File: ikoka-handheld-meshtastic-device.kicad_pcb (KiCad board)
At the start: 2 copper layers, 40 x 55 mm, 40 parts, among them J1 Conn_Coaxial, J4 1.25-2PWB, Q1 AO3401A, SW1 SW_Push, SW2 SW_Push, U1 MT3608, U2 E22-900M30S, U3 XIAO-nRF52840-SMD, U4 TP4056-42-ESOP8

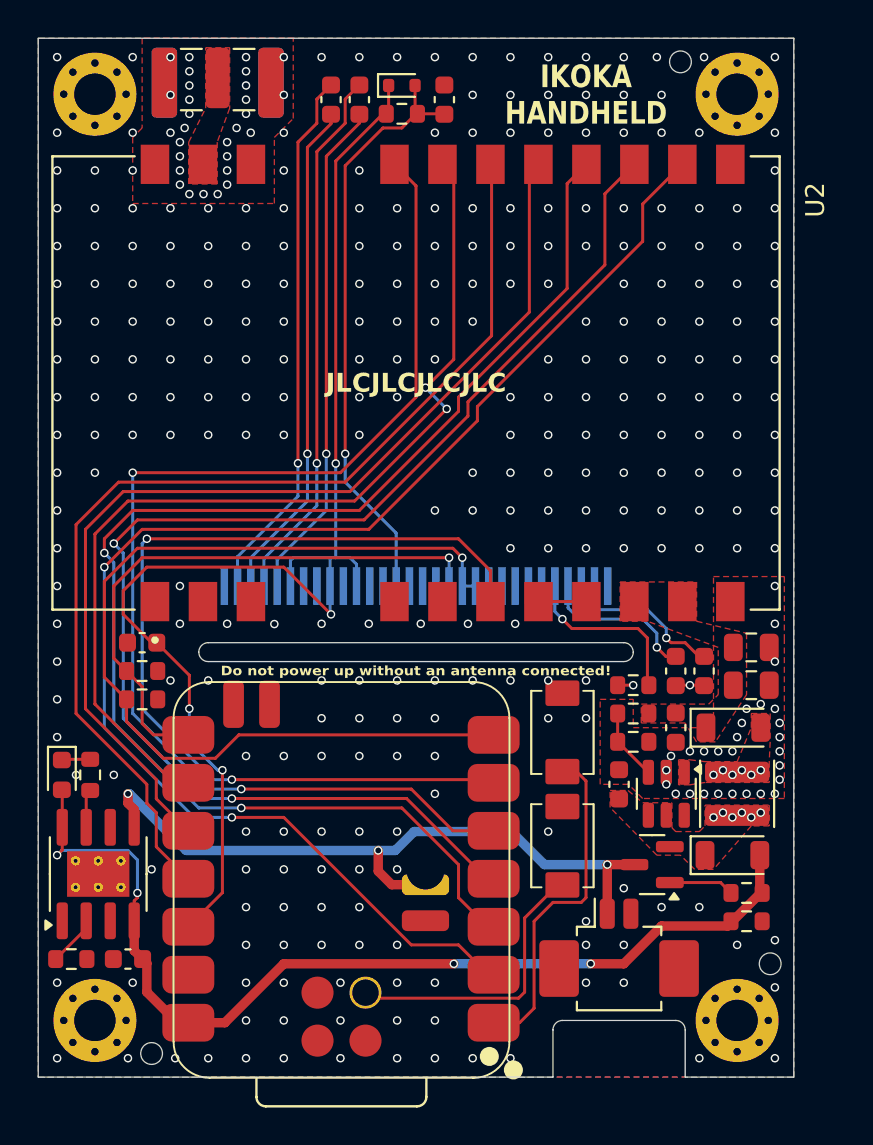
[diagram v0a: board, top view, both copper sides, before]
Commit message: fix: Add BAT output capacitor on TP4056
Signed-off-by: Andrew Yong <me@ndoo.sg>
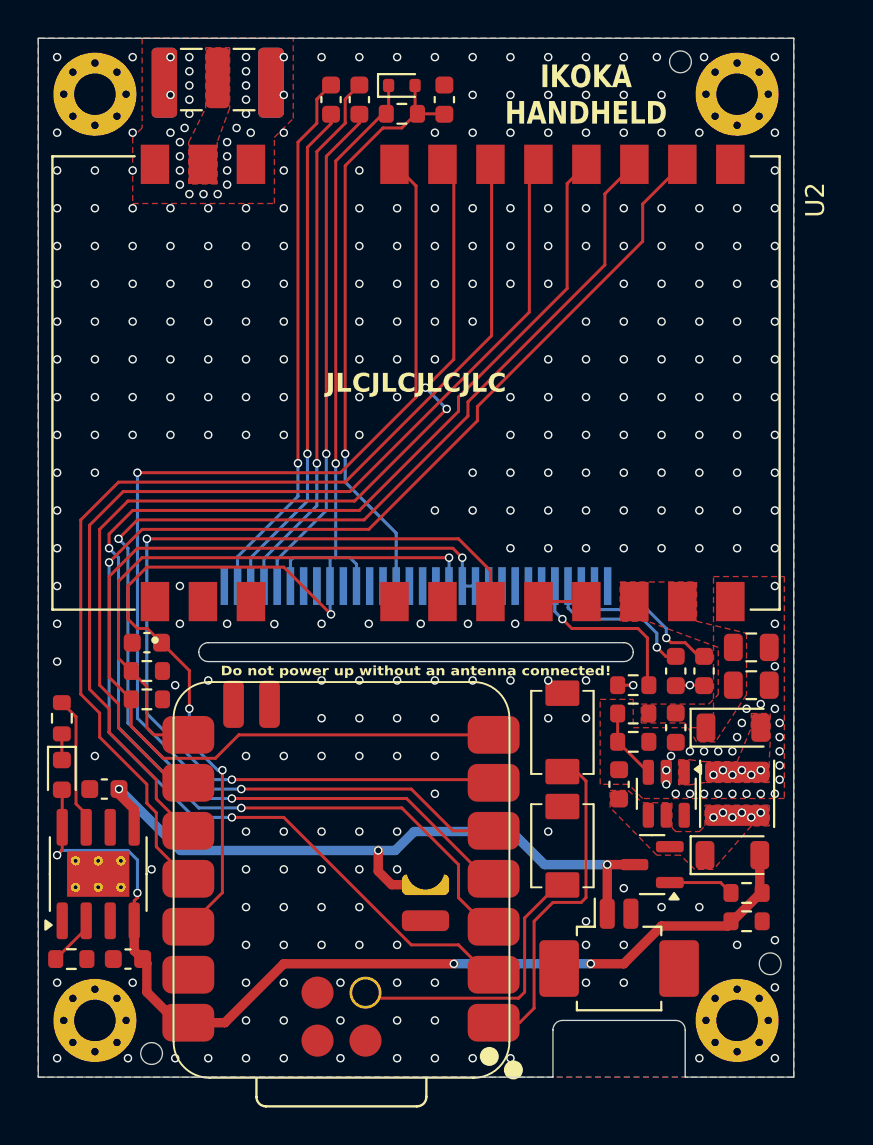
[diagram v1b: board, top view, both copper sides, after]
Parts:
- added C12: 10uF, Capacitor_SMD:C_0603_1608Metric, F.Cu at (133.5, 84.8)
- moved R10 3.35 mm to (131.2, 81.0), turned to 90 degrees
- moved C5 0.25 mm to (135.8, 77.0)
- moved R6 0.25 mm to (135.8, 80.0)
- moved R7 0.25 mm to (135.8, 78.5)
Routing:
- net Net-(U4-~{CHRG}): track 2.07 -> 7.13 mm
- net +BATT: track 37.6 -> 38.6 mm
- net GND: vias 347 -> 344

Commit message: fix: Flip SSD1306 footprint (fixes #1)
Signed-off-by: Andrew Yong <me@ndoo.sg>
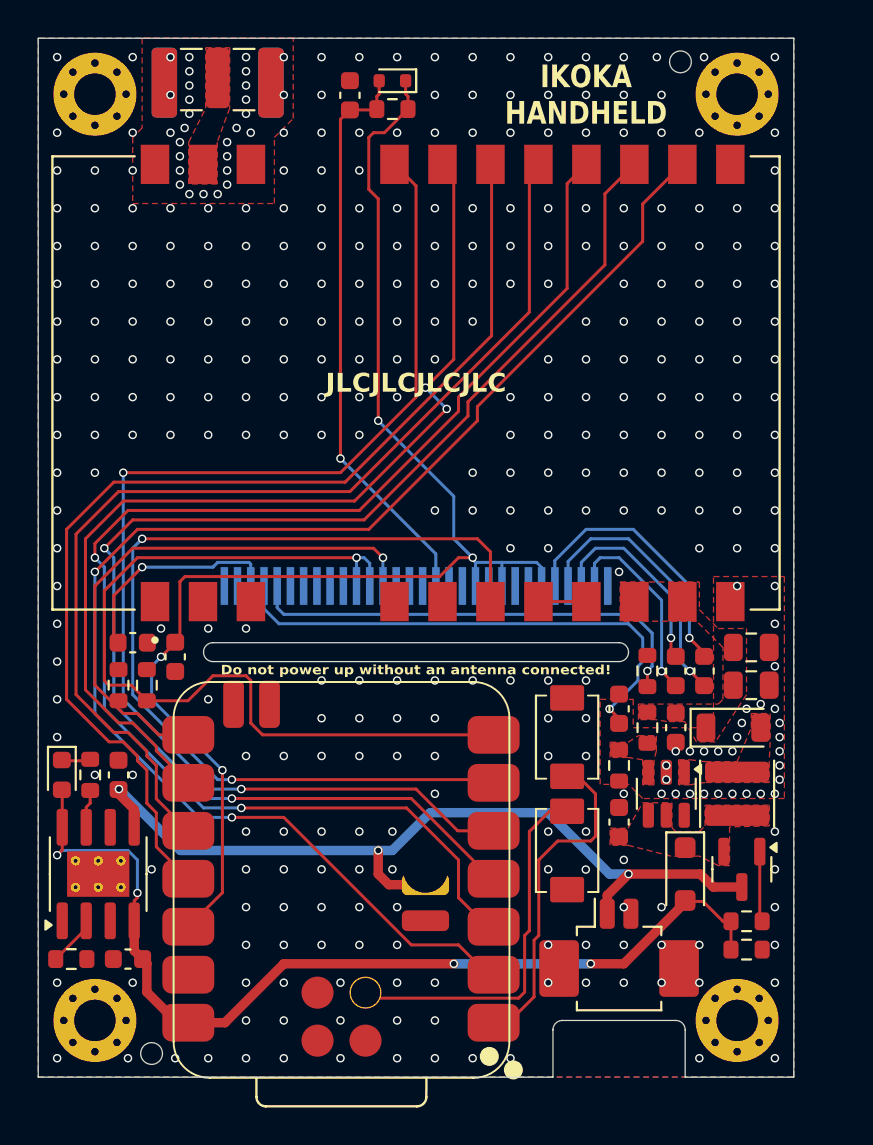
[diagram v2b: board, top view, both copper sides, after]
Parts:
- DS1: footprint Display:OLED-128O064D -> Display:OLED-128O064D_ReverseMount
- moved C8 35.3 mm to (165.2, 78.5), turned to -90 degrees
- moved C9 35.3 mm to (163.8, 78.5), turned to -90 degrees
- moved C6 30.3 mm to (135.0, 77.0), turned to 0 degrees
- moved C10 5.01 mm to (146.5, 48.0)
- moved Q1 4.76 mm to (167.2, 89.0), turned to -90 degrees
- moved C7 3.61 mm to (160.8, 80.5), turned to 90 degrees
- moved R10 3.35 mm to (132.8, 84.0), turned to -90 degrees
- moved D3 2.69 mm to (164.2, 89.2), turned to -90 degrees
- moved C1 2.00 mm to (160.8, 86.5)
- moved C5 1.68 mm to (137.2, 77.8), turned to -90 degrees
- moved R7 1.68 mm to (134.2, 79.2), turned to 90 degrees
- moved R3 1.50 mm to (167.5, 93.2)
- moved R4 1.50 mm to (167.5, 91.8), turned to 0 degrees
- moved R2 1.46 mm to (160.8, 83.5), turned to -90 degrees
- moved C12 1.06 mm to (134.2, 84.0), turned to 90 degrees
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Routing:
- net Net-(DS1-VCOMH): track 8.36 -> 27.4 mm
- net Net-(DS1-C2N): track 28.6 -> 10.6 mm
- net Net-(DS1-C2P): track 26.7 -> 10.7 mm
- net Net-(DS1-IREF): track 9.36 -> 24.5 mm
- net Net-(DS1-C1P): track 28.6 -> 14.4 mm
- net Net-(DS1-C1N): track 26.8 -> 14.5 mm
- net +BATT: track 38.6 -> 45.7 mm
- net +5V: track 57.8 -> 51.7 mm
- net Net-(U4-~{CHRG}): track 7.13 -> 2.04 mm
- net +3V3: track 69.0 -> 73.4 mm
- net /RESET: track 15.4 -> 19.7 mm
- net /I2C_SDA: track 50.5 -> 46.6 mm
- net Net-(U1-FB): track 3.79 -> 0.00 mm
- net Net-(DS1-VCC): track 9.02 -> 11.8 mm
- net GND: track 2.35 -> 0.21 mm, vias 344 -> 365
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- added copper zone on F.Cu, net Net-(U1-FB)
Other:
- outline, holes or cut-outs redrawn

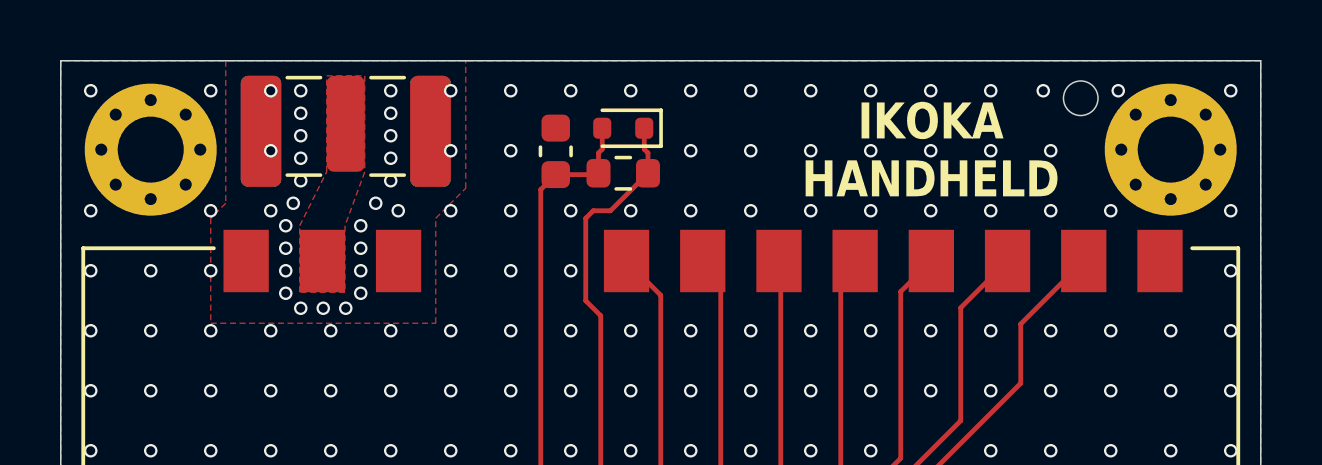
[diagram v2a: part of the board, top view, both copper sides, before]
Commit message: fix(pcbnew): Add user drawings for dimensions and fix hole alignment
Signed-off-by: Andrew Yong <me@ndoo.sg>
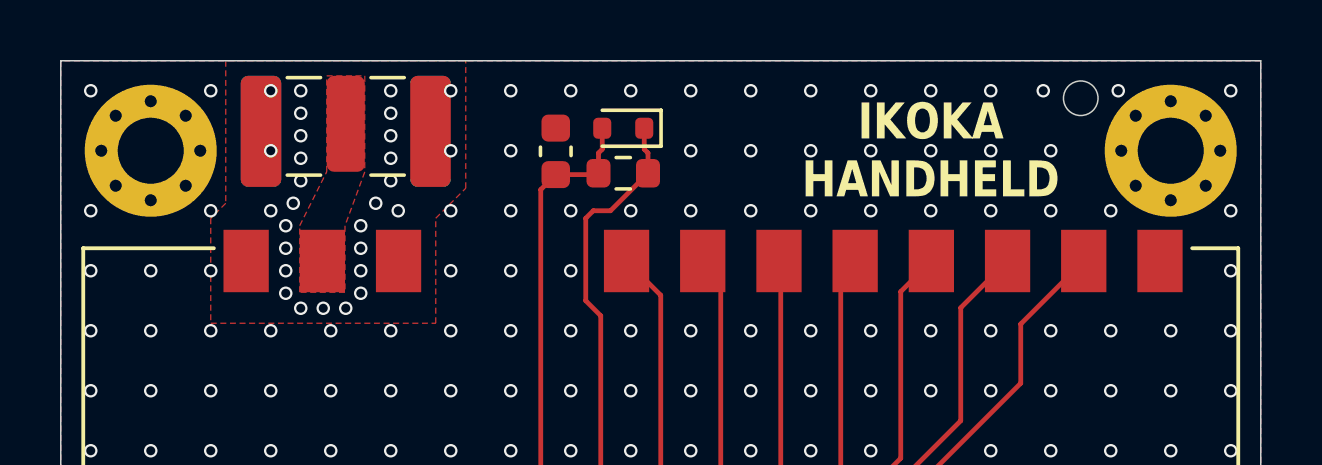
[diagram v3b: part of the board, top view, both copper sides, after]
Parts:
- turned H2 to 0 degrees
- turned H1 to 0 degrees

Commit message: feat: Change TP4056 charge current from 1A to 780mA
For a total of 880mA (780mA TP4056 + 100mA onboard XIAO charger).

Most pouch cells the size of the PCB are around 1000mAh, and 1.1A charge rate is above 1C for these cells, which will increase battery wear.

Signed-off-by: Andrew Yong <me@ndoo.sg>
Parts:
- R9: value 1.2k -> 1.5k
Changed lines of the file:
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@@
 			)
 		)
-		(property "Value" "1.2k"
+		(property "Value" "1.5k"
 			(at 0 1.43 0)
 			(layer "F.Fab")
@@
 			)
 		)
-		(property "LCSC" "C22765"
+		(property "LCSC" "C22843"
 			(at 0 0 0)
 			(unlocked yes)

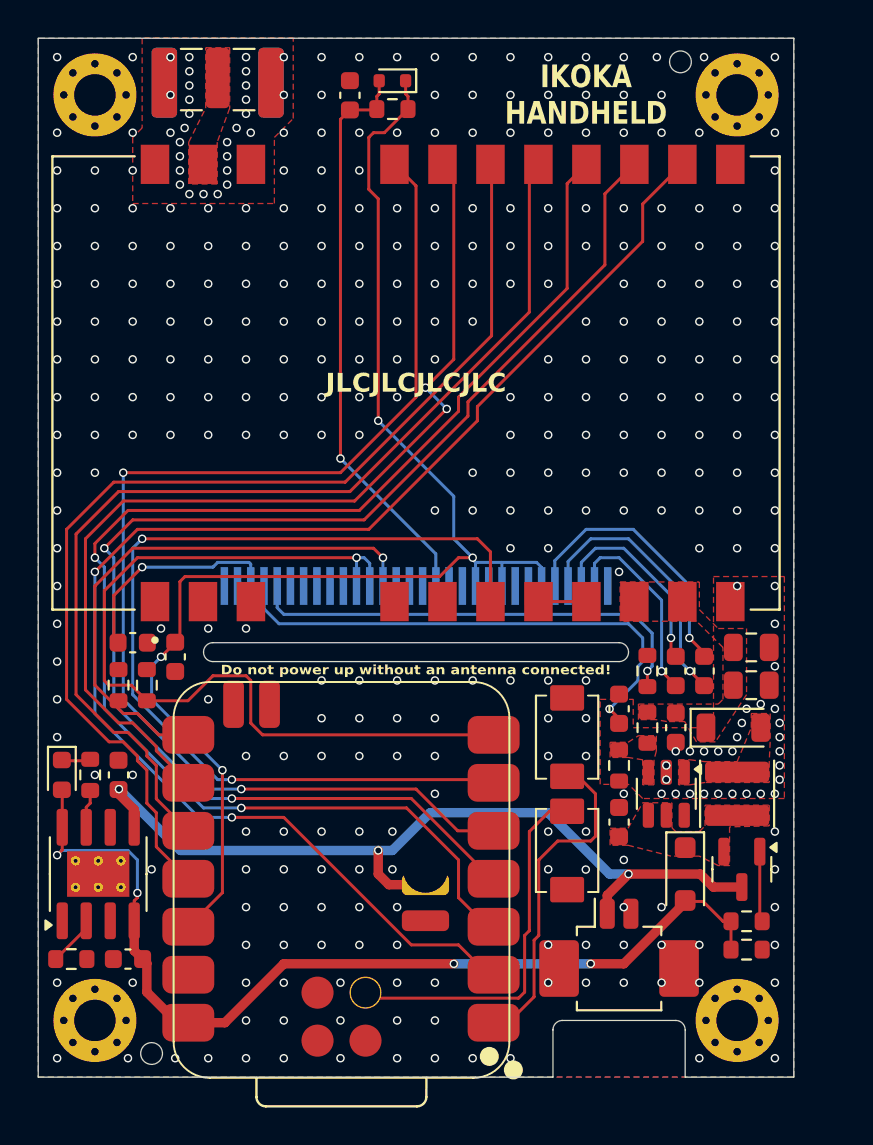
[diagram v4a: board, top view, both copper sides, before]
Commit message: fix: Change inductor from 22uH to 2.2uH, Move XIAO up 0.1mm
- Change inductor from 22uH to 2.2uH
  - From: FTC303015D220MBCA
  - To: FNR3015S2R2MT
  - Lower DCR
  - Higher current headroom
  - Better transient response
- Move XIAO module up 0.1mm for better PCB edge clearance

Signed-off-by: Andrew Yong <me@ndoo.sg>
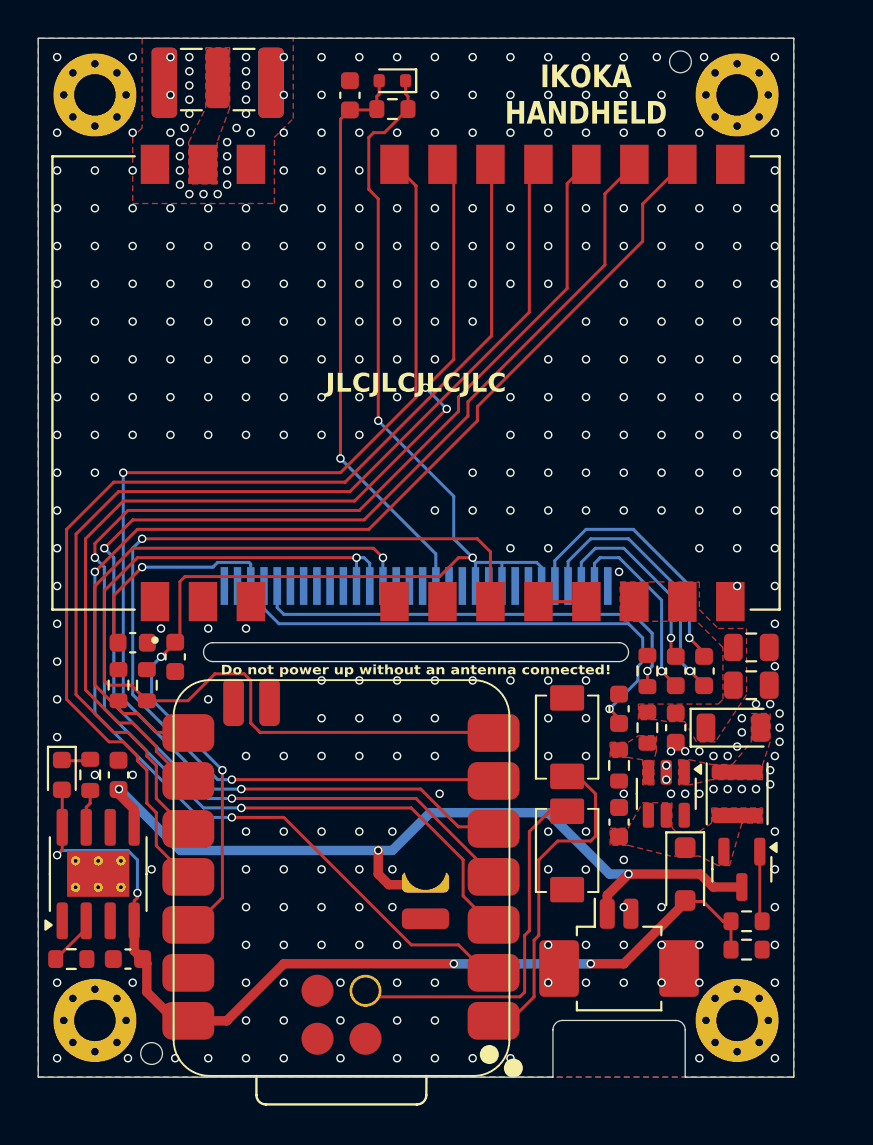
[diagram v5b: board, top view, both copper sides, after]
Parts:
- L1: value FTC303015D220MBCA -> FNR3015S2R2MT; footprint Inductor_SMD:L_Wuerth_MAPI-3015 -> Inductor_SMD:L_Changjiang_FNR3015S
- U3: footprint Seeed Studio XIAO Series Library:XIAO-nRF52840-SMD -> Seeed Studio XIAO Series Library:XIAO-nRF52840-SMD_Handsoldering
- moved U3 0.10 mm to (146.0, 89.4)
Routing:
- net GND: vias 365 -> 364
